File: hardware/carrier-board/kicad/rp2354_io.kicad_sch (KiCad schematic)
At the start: 0 parts

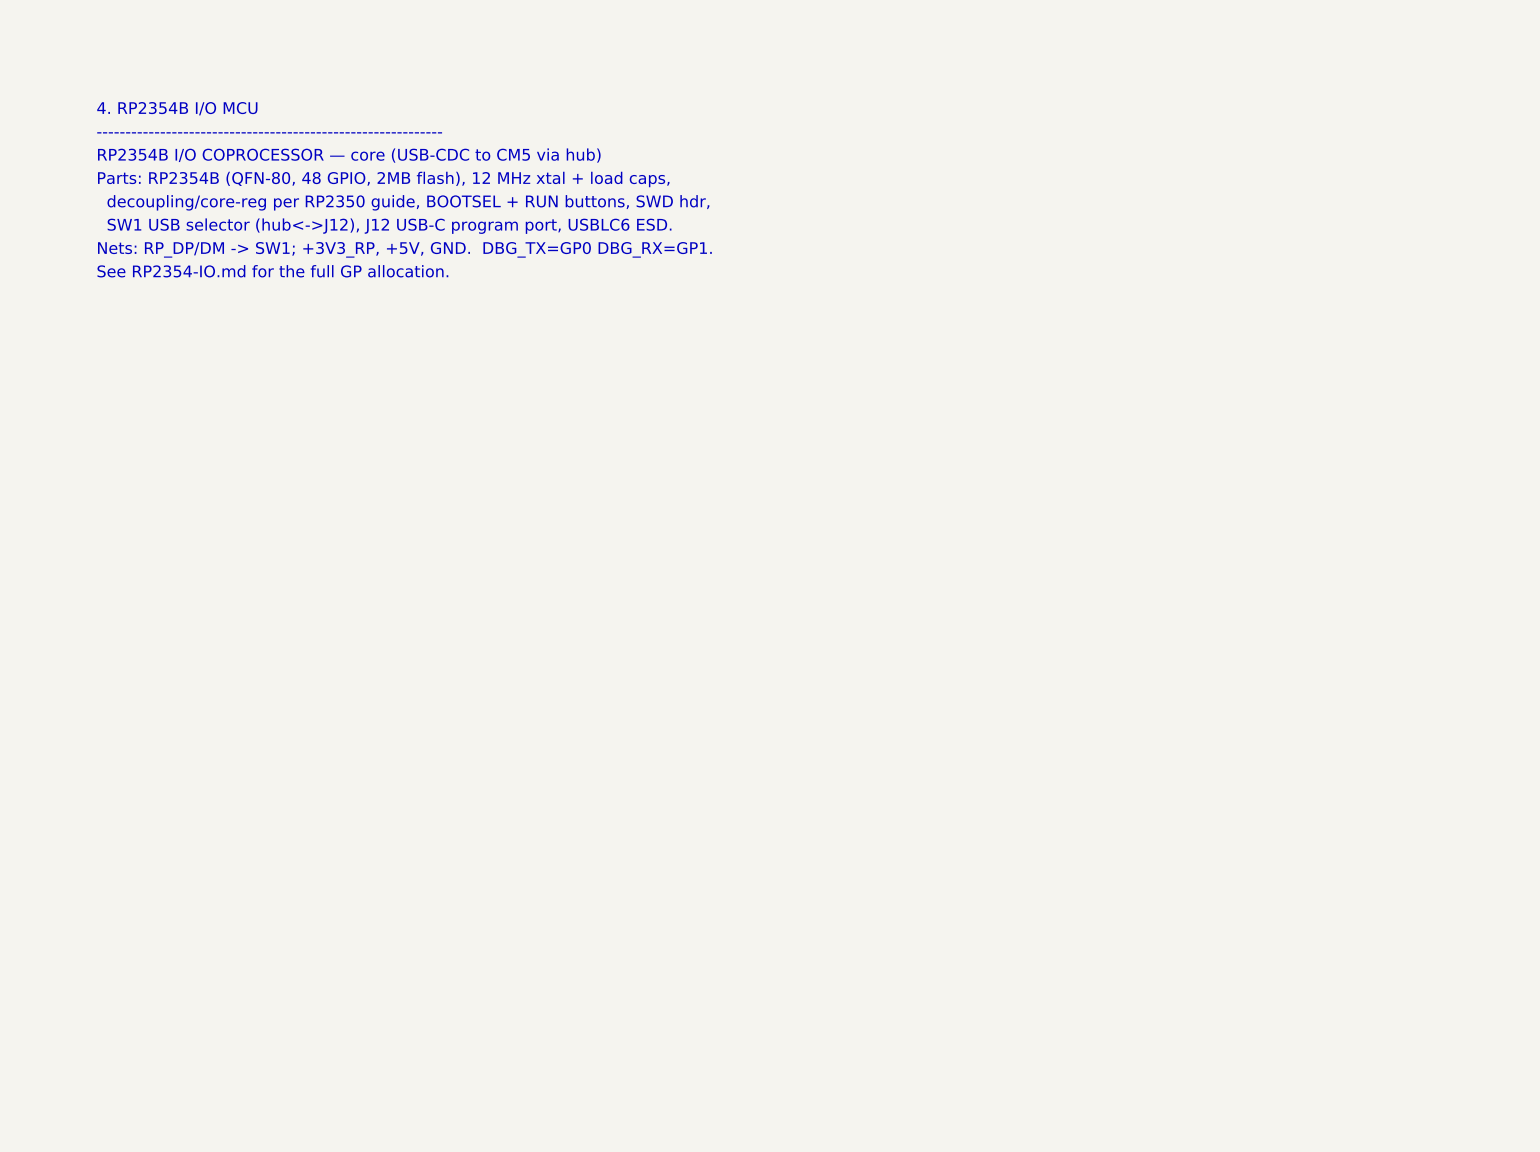
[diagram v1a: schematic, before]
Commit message: Carrier KiCad: populate all 11 schematic sheets
Replace populate_face_buffer.py with populate_sheets.py: one generator that
emits all 11 populated sub-sheets reusing the KiCad-9 format proven by the
face_buffer proof. Shared symbol library + generic box-symbol builder; condensed
CM5 (2x DF40-100) and RP2354B (QFN-80) symbols showing only used pins.

Connectivity by net labels (global for rails + cross-sheet nets: GPIOxx HUB75,
MX_*, LED*_DAT, SRV*, BTN*, *_USB_*; local within-sheet). Sheets: power
(protection + rails + AP2112 +3V3_RP), cm5 (HUB75 out + fan MOSFETs + RP ctrl),
face_buffer, rp2354_io (RP2354B + xtal + SW1/J12 + ESD + SWD), rp2354_face
(U10->J3), leds (U11 quad ->J4a-d), sensors_i2c (pull-ups+J5+STEMMA),
servos (J20-27 + rail), gpio_buttons (J6), usb (USB2514B hub + uplink),
cameras_display (CSI FFC + HDMI).

Verified: all sheets paren-balanced, every used lib_id defined, all instance
paths match sheet UUIDs, root<->sub-sheet UUID linkage intact. generate_skeleton.py
now lists all sheets POPULATED (writes only root+project). Not yet opened in
KiCad here -- expect ERC warnings (PWR_FLAG, unconnected pins) to clean.
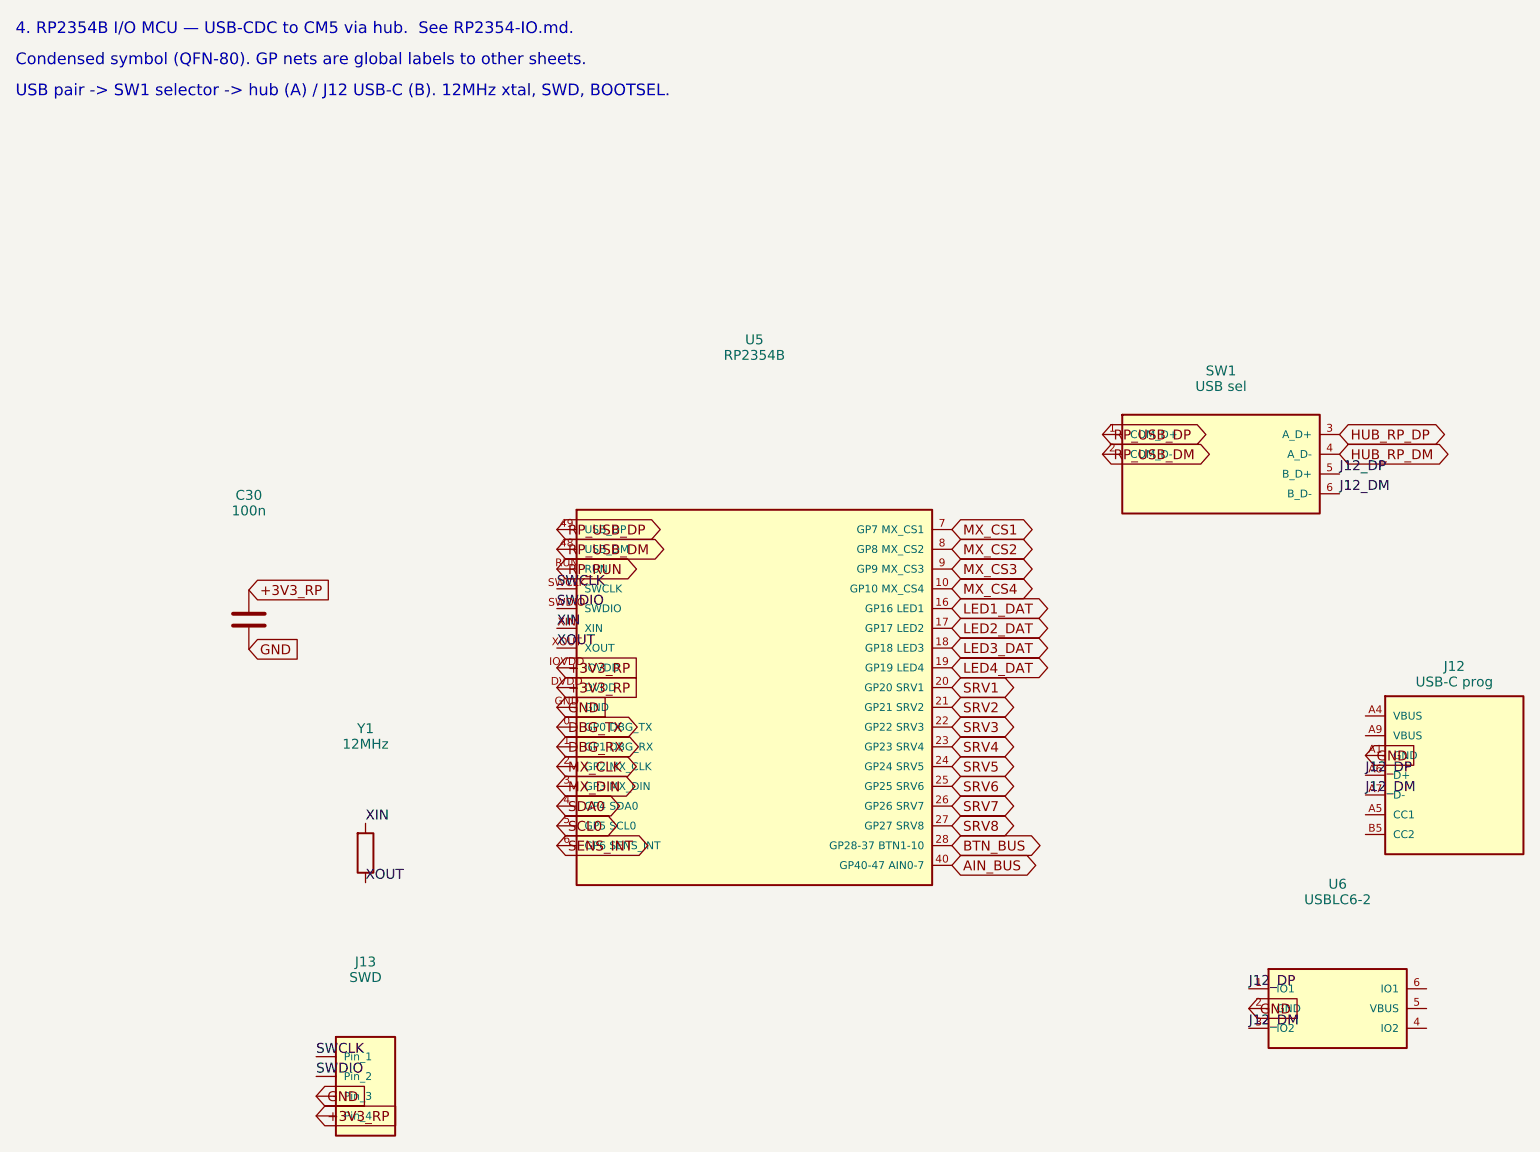
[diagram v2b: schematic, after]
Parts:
- added C30: 100n, symbol Device:C
- added J12: USB-C prog, symbol Connector:USB_C_Receptacle_USB2.0
- added J13: SWD, symbol Connector_Generic:Conn_01x04
- added SW1: USB sel, symbol Connector:USB_Selector
- added U5: RP2354B, symbol MCU_RaspberryPi:RP2354B
- added U6: USBLC6-2, symbol Interface_USB:USBLC6-2SC6
- added Y1: 12MHz, symbol Device:Crystal
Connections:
- new net +3V3_RP: C30.1, J13.4 (Pin_4), U5.DVDD, U5.IOVDD
- new net AIN_BUS: U5.40 (GP40-47 AIN0-7)
- new net BTN_BUS: U5.28 (GP28-37 BTN1-10)
- new net DBG_RX: U5.1 (GP1 DBG_RX)
- new net DBG_TX: U5.0 (GP0 DBG_TX)
- new net GND: C30.2, J12.A1 (GND), J13.3 (Pin_3), U5.GND, U6.2 (GND)
- new net HUB_RP_DM: SW1.4 (A_D-)
- new net HUB_RP_DP: SW1.3 (A_D+)
- new net J12_DM: J12.A7 (D-), SW1.6 (B_D-), U6.3 (IO2)
- new net J12_DP: J12.A6 (D+), SW1.5 (B_D+), U6.1 (IO1)
- new net LED1_DAT: U5.16 (GP16 LED1)
- new net LED2_DAT: U5.17 (GP17 LED2)
- new net LED3_DAT: U5.18 (GP18 LED3)
- new net LED4_DAT: U5.19 (GP19 LED4)
- new net MX_CLK: U5.2 (GP2 MX_CLK)
- new net MX_CS1: U5.7 (GP7 MX_CS1)
- new net MX_CS2: U5.8 (GP8 MX_CS2)
- new net MX_CS3: U5.9 (GP9 MX_CS3)
- new net MX_CS4: U5.10 (GP10 MX_CS4)
- new net MX_DIN: U5.3 (GP3 MX_DIN)
- new net RP_RUN: U5.RUN
- new net RP_USB_DM: SW1.2 (COM_D-), U5.48 (USB_DM)
- new net RP_USB_DP: SW1.1 (COM_D+), U5.49 (USB_DP)
- new net SCL0: U5.5 (GP5 SCL0)
- new net SDA0: U5.4 (GP4 SDA0)
- new net SENS_INT: U5.6 (GP6 SENS_INT)
- new net SRV1: U5.20 (GP20 SRV1)
- new net SRV2: U5.21 (GP21 SRV2)
- new net SRV3: U5.22 (GP22 SRV3)
- new net SRV4: U5.23 (GP23 SRV4)
- new net SRV5: U5.24 (GP24 SRV5)
- new net SRV6: U5.25 (GP25 SRV6)
- new net SRV7: U5.26 (GP26 SRV7)
- new net SRV8: U5.27 (GP27 SRV8)
- new net SWCLK: J13.1 (Pin_1), U5.SWCLK
- new net SWDIO: J13.2 (Pin_2), U5.SWDIO
- new net XIN: U5.XIN, Y1.1
- new net XOUT: U5.XOUT, Y1.2
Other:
- note added: "4. RP2354B I/O MCU — USB-CDC to CM5 via hub. See RP2354-IO.md."
- note added: "Condensed symbol (QFN-80). GP nets are global labels to other sheets."
- note added: "USB pair -> SW1 selector -> hub (A) / J12 USB-C (B). 12MHz xtal, SWD, BOOTSEL."
- note removed: "------------------------------------------------------------"
- note removed: "4. RP2354B I/O MCU"
- note removed: "Nets: RP_DP/DM -> SW1; +3V3_RP, +5V, GND. DBG_TX=GP0 DBG_RX=GP1."
- note removed: "Parts: RP2354B (QFN-80, 48 GPIO, 2MB flash), 12 MHz xtal + load caps,"
- note removed: "RP2354B I/O COPROCESSOR — core (USB-CDC to CM5 via hub)"
- note removed: "SW1 USB selector (hub<->J12), J12 USB-C program port, USBLC6 ESD."
- note removed: "See RP2354-IO.md for the full GP allocation."
- note removed: "decoupling/core-reg per RP2350 guide, BOOTSEL + RUN buttons, SWD hdr,"
